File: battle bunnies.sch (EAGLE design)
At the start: 60 parts, among them IC1 CP2104, Q1 mmbt2222, Q2 mmbt2222, SW2 KMR2, U1 PCA9685, U2 SPX3819, U3 MCP73831T-2ACI/OT, X2 ESP-12, X4 20329

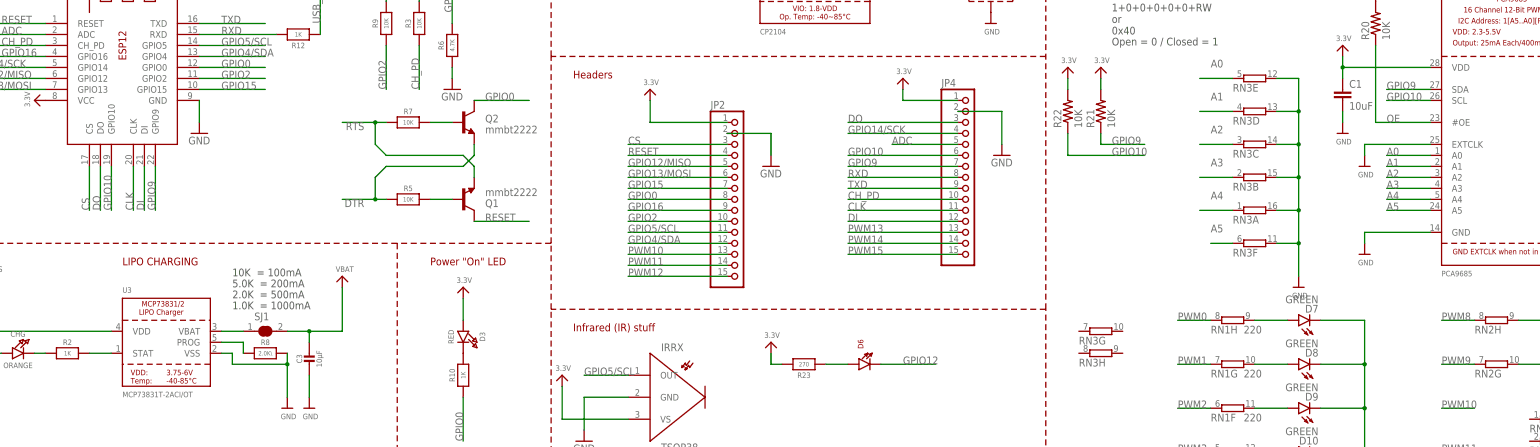
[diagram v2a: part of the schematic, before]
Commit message: Reworking things + the ESP12S is lacking pins present on the schematic (doh)
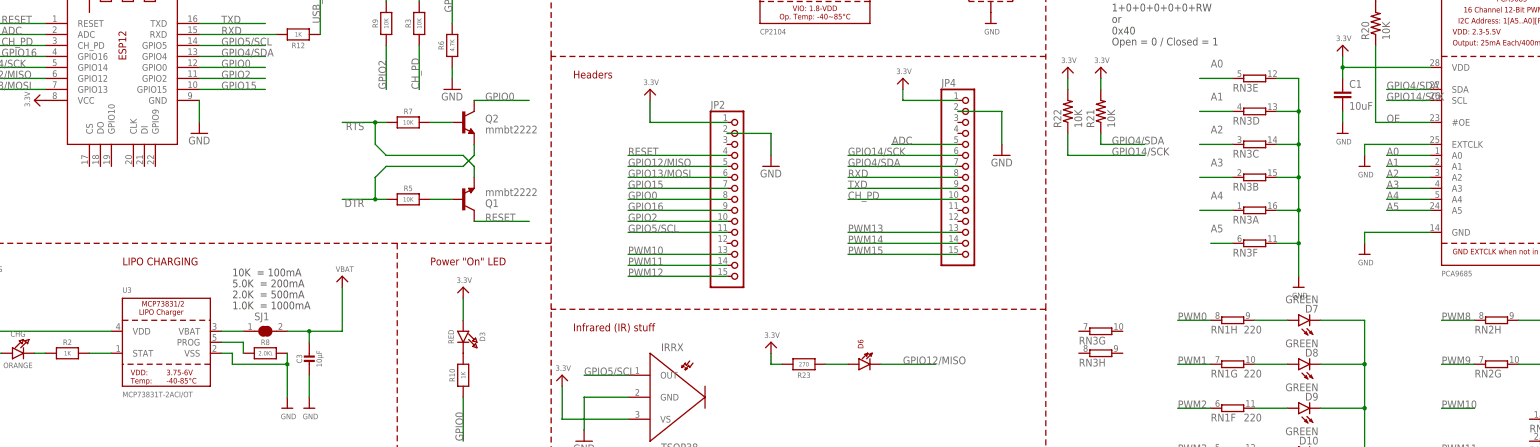
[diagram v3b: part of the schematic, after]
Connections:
- removed net CLK: JP4.11, X2.CLK
- removed net CS: JP2.3, X2.CS
- removed net DI: JP4.12, X2.DI
- removed net DO: JP4.3, X2.DO
- removed net GPIO10: JP4.6, R22.1, U1.SCL, X2.GPIO10
- removed net GPIO12: D6.C
- removed net GPIO9: JP4.7, R21.1, U1.SDA, X2.GPIO9
- net GPIO12/MISO: now also D6.C
- net GPIO14/SCK: now also JP4.6, R22.1, U1.SCL; no longer JP4.4
- net GPIO4/SDA: now also JP4.7, R21.1, U1.SDA; no longer JP2.12
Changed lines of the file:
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@@
 <net name="GPIO4/SDA" class="0">
-<segment>
-<wire x1="154.94" y1="144.78" x2="177.8" y2="144.78" width="0.1524" layer="91"/>
-<label x="154.94" y="144.78" size="1.778" layer="95"/>
-<pinref part="JP2" gate="A" pin="12"/>
-</segment>
 <segment>
 <pinref part="X2" gate="G$1" pin="GPIO4"/>
@@
 <label x="60.96" y="187.96" size="1.778" layer="95"/>
 </segment>
+<segment>
+<wire x1="264.16" y1="167.64" x2="264.16" y2="170.18" width="0.1524" layer="91"/>
+<label x="266.7" y="167.64" size="1.778" layer="95"/>
+<pinref part="R21" gate="G$1" pin="1"/>
+<wire x1="264.16" y1="167.64" x2="274.32" y2="167.64" width="0.1524" layer="91"/>
+</segment>
+<segment>
+<wire x1="340.36" y1="180.34" x2="330.2" y2="180.34" width="0.1524" layer="91"/>
+<label x="330.2" y="180.34" size="1.778" layer="95"/>
+<pinref part="U1" gate="G$1" pin="SDA"/>
+</segment>
+<segment>
+<pinref part="JP4" gate="A" pin="7"/>
+<wire x1="231.14" y1="162.56" x2="205.74" y2="162.56" width="0.1524" layer="91"/>
+<label x="205.74" y="162.56" size="1.778" layer="95"/>
+</segment>
 </net>
 <net name="GPIO2" class="0">
@@
 <wire x1="2.54" y1="185.42" x2="20.32" y2="185.42" width="0.1524" layer="91"/>
 <label x="2.54" y="185.42" size="1.778" layer="95"/>
-</segment>
-<segment>
-<wire x1="231.14" y1="170.18" x2="205.74" y2="170.18" width="0.1524" layer="91"/>
-<label x="205.74" y="170.18" size="1.778" layer="95"/>
-<pinref part="JP4" gate="A" pin="4"/>
-</segment>
-</net>
-<net name="GPIO13/MOSI" class="0">
-<segment>
-<pinref part="X2" gate="G$1" pin="GPIO13"/>
-<wire x1="2.54" y1="180.34" x2="20.32" y2="180.34" width="0.1524" layer="91"/>
-<label x="2.54" y="180.34" size="1.778" layer="95"/>
-</segment>
-<segment>
-<wire x1="177.8" y1="160.02" x2="154.94" y2="160.02" width="0.1524" layer="91"/>
-<label x="154.94" y="160.02" size="1.778" layer="95"/>
-<pinref part="JP2" gate="A" pin="6"/>
-</segment>
-<segment>
-<wire x1="172.72" y1="63.5" x2="190.5" y2="63.5" width="0.1524" layer="91"/>
-<label x="177.8" y="63.5" size="1.778" layer="95"/>
-<pinref part="S2" gate="G$1" pin="2"/>
-</segment>
-</net>
-<net name="GPIO12/MISO" class="0">
-<segment>
-<pinref part="X2" gate="G$1" pin="GPIO12"/>
-<wire x1="20.32" y1="182.88" x2="2.54" y2="182.88" width="0.1524" layer="91"/>
-<label x="2.54" y="182.88" size="1.778" layer="95"/>
-</segment>
-<segment>
-<wire x1="154.94" y1="162.56" x2="177.8" y2="162.56" width="0.1524" layer="91"/>
-<label x="154.94" y="162.56" size="1.778" layer="95"/>
-<pinref part="JP2" gate="A" pin="5"/>
-</segment>
-</net>
-<net name="USB_RX" class="0">
-<segment>
-<pinref part="R12" gate="G$1" pin="1"/>
-<wire x1="83.82" y1="193.04" x2="83.82" y2="205.74" width="0.1524" layer="91"/>
-<label x="83.82" y="195.58" size="1.778" layer="95" rot="R90"/>
-</segment>
-<segment>
-<wire x1="213.36" y1="210.82" x2="226.06" y2="210.82" width="0.1524" layer="91"/>
-<pinref part="IC1" gate="G$1" pin="TXD"/>
-<label x="215.9" y="210.82" size="1.778" layer="95"/>
-</segment>
-</net>
-<net name="N$9" class="0">
-<segment>
-<pinref part="U3" gate="G$1" pin="VBAT"/>
-<pinref part="SJ1" gate="G$1" pin="1"/>
-<wire x1="66.04" y1="124.46" x2="60.96" y2="124.46" width="0.1524" layer="91"/>
-</segment>
-</net>
-<net name="N$11" class="0">
-<segment>
-<wire x1="68.58" y1="241.3" x2="73.66" y2="241.3" width="0.1524" layer="91"/>
-<pinref part="D4" gate="G$1" pin="A"/>
-</segment>
-</net>
-<net name="GPIO10" class="0">
-<segment>
-<pinref part="X2" gate="G$1" pin="GPIO10"/>
-<wire x1="35.56" y1="162.56" x2="35.56" y2="152.4" width="0.1524" layer="91"/>
-<label x="35.56" y="152.4" size="1.778" layer="95" rot="R90"/>
 </segment>
 <segment>
@@
 </segment>
 <segment>
+<pinref part="JP4" gate="A" pin="6"/>
 <wire x1="231.14" y1="165.1" x2="205.74" y2="165.1" width="0.1524" layer="91"/>
 <label x="205.74" y="165.1" size="1.778" layer="95"/>
-<pinref part="JP4" gate="A" pin="6"/>
-</segment>
-</net>
-<net name="GPIO9" class="0">
-<segment>
-<pinref part="X2" gate="G$1" pin="GPIO9"/>
-<wire x1="45.72" y1="162.56" x2="45.72" y2="152.4" width="0.1524" layer="91"/>
-<label x="45.72" y="152.4" size="1.778" layer="95" rot="R90"/>
-</segment>
-<segment>
-<wire x1="264.16" y1="167.64" x2="264.16" y2="170.18" width="0.1524" layer="91"/>
-<label x="266.7" y="167.64" size="1.778" layer="95"/>
-<pinref part="R21" gate="G$1" pin="1"/>
-<wire x1="264.16" y1="167.64" x2="274.32" y2="167.64" width="0.1524" layer="91"/>
-</segment>
-<segment>
-<wire x1="340.36" y1="180.34" x2="330.2" y2="180.34" width="0.1524" layer="91"/>
-<label x="330.2" y="180.34" size="1.778" layer="95"/>
-<pinref part="U1" gate="G$1" pin="SDA"/>
-</segment>
-<segment>
-<wire x1="231.14" y1="162.56" x2="205.74" y2="162.56" width="0.1524" layer="91"/>
-<label x="205.74" y="162.56" size="1.778" layer="95"/>
-<pinref part="JP4" gate="A" pin="7"/>
+</segment>
+</net>
+<net name="GPIO13/MOSI" class="0">
+<segment>
+<pinref part="X2" gate="G$1" pin="GPIO13"/>
+<wire x1="2.54" y1="180.34" x2="20.32" y2="180.34" width="0.1524" layer="91"/>
+<label x="2.54" y="180.34" size="1.778" layer="95"/>
+</segment>
+<segment>
+<wire x1="177.8" y1="160.02" x2="154.94" y2="160.02" width="0.1524" layer="91"/>
+<label x="154.94" y="160.02" size="1.778" layer="95"/>
+<pinref part="JP2" gate="A" pin="6"/>
+</segment>
+<segment>
+<wire x1="172.72" y1="63.5" x2="190.5" y2="63.5" width="0.1524" layer="91"/>
+<label x="177.8" y="63.5" size="1.778" layer="95"/>
+<pinref part="S2" gate="G$1" pin="2"/>
+</segment>
+</net>
+<net name="GPIO12/MISO" class="0">
+<segment>
+<pinref part="X2" gate="G$1" pin="GPIO12"/>
+<wire x1="20.32" y1="182.88" x2="2.54" y2="182.88" width="0.1524" layer="91"/>
+<label x="2.54" y="182.88" size="1.778" layer="95"/>
+</segment>
+<segment>
+<wire x1="154.94" y1="162.56" x2="177.8" y2="162.56" width="0.1524" layer="91"/>
+<label x="154.94" y="162.56" size="1.778" layer="95"/>
+<pinref part="JP2" gate="A" pin="5"/>
+</segment>
+<segment>
+<pinref part="D6" gate="G$1" pin="C"/>
+<wire x1="213.36" y1="116.84" x2="226.06" y2="116.84" width="0.1524" layer="91"/>
+<label x="218.44" y="116.84" size="1.778" layer="95"/>
+</segment>
+</net>
+<net name="USB_RX" class="0">
+<segment>
+<pinref part="R12" gate="G$1" pin="1"/>
+<wire x1="83.82" y1="193.04" x2="83.82" y2="205.74" width="0.1524" layer="91"/>
+<label x="83.82" y="195.58" size="1.778" layer="95" rot="R90"/>
+</segment>
+<segment>
+<wire x1="213.36" y1="210.82" x2="226.06" y2="210.82" width="0.1524" layer="91"/>
+<pinref part="IC1" gate="G$1" pin="TXD"/>
+<label x="215.9" y="210.82" size="1.778" layer="95"/>
+</segment>
+</net>
+<net name="N$9" class="0">
+<segment>
+<pinref part="U3" gate="G$1" pin="VBAT"/>
+<pinref part="SJ1" gate="G$1" pin="1"/>
+<wire x1="66.04" y1="124.46" x2="60.96" y2="124.46" width="0.1524" layer="91"/>
+</segment>
+</net>
+<net name="N$11" class="0">
+<segment>
+<wire x1="68.58" y1="241.3" x2="73.66" y2="241.3" width="0.1524" layer="91"/>
+<pinref part="D4" gate="G$1" pin="A"/>
 </segment>
 </net>
@@
 </segment>
 </net>
-<net name="GPIO12" class="0">
-<segment>
-<pinref part="D6" gate="G$1" pin="C"/>
-<wire x1="213.36" y1="116.84" x2="226.06" y2="116.84" width="0.1524" layer="91"/>
-<label x="218.44" y="116.84" size="1.778" layer="95"/>
-</segment>
-</net>
-<net name="CS" class="0">
-<segment>
-<pinref part="X2" gate="G$1" pin="CS"/>
-<wire x1="30.48" y1="162.56" x2="30.48" y2="152.4" width="0.1524" layer="91"/>
-<label x="30.48" y="152.4" size="1.778" layer="95" rot="R90"/>
-</segment>
-<segment>
-<pinref part="JP2" gate="A" pin="3"/>
-<wire x1="177.8" y1="167.64" x2="154.94" y2="167.64" width="0.1524" layer="91"/>
-<label x="154.94" y="167.64" size="1.778" layer="95"/>
-</segment>
-</net>
-<net name="DO" class="0">
-<segment>
-<pinref part="X2" gate="G$1" pin="DO"/>
-<wire x1="33.02" y1="162.56" x2="33.02" y2="152.4" width="0.1524" layer="91"/>
-<label x="33.02" y="152.4" size="1.778" layer="95" rot="R90"/>
-</segment>
-<segment>
-<pinref part="JP4" gate="A" pin="3"/>
-<wire x1="231.14" y1="172.72" x2="205.74" y2="172.72" width="0.1524" layer="91"/>
-<label x="205.74" y="172.72" size="1.778" layer="95"/>
-</segment>
-</net>
-<net name="CLK" class="0">
-<segment>
-<pinref part="X2" gate="G$1" pin="CLK"/>
-<wire x1="40.64" y1="162.56" x2="40.64" y2="152.4" width="0.1524" layer="91"/>
-<label x="40.64" y="152.4" size="1.778" layer="95" rot="R90"/>
-</segment>
-<segment>
-<wire x1="231.14" y1="152.4" x2="205.74" y2="152.4" width="0.1524" layer="91"/>
-<label x="205.74" y="152.4" size="1.778" layer="95"/>
-<pinref part="JP4" gate="A" pin="11"/>
-</segment>
-</net>
-<net name="DI" class="0">
-<segment>
-<pinref part="X2" gate="G$1" pin="DI"/>
-<wire x1="43.18" y1="162.56" x2="43.18" y2="152.4" width="0.1524" layer="91"/>
-<label x="43.18" y="152.4" size="1.778" layer="95" rot="R90"/>
-</segment>
-<segment>
-<wire x1="231.14" y1="149.86" x2="205.74" y2="149.86" width="0.1524" layer="91"/>
-<label x="205.74" y="149.86" size="1.778" layer="95"/>
-<pinref part="JP4" gate="A" pin="12"/>
-</segment>
-</net>

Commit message: more cleanups
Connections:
- net GPIO0: now also JP2.3; no longer JP2.8
- net GPIO12/MISO: now also JP2.12; no longer JP2.5
- net GPIO2: now also JP2.4; no longer JP2.10
- net RESET: now also JP2.5; no longer JP2.4
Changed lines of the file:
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@@
 <?xml version="1.0" encoding="utf-8"?>
 <!DOCTYPE eagle SYSTEM "eagle.dtd">
-<eagle version="7.6.0">
+<eagle version="7.7.0">
 <drawing>
 <settings>
@@
 </segment>
 <segment>
-<pinref part="JP2" gate="A" pin="4"/>
-<wire x1="177.8" y1="165.1" x2="154.94" y2="165.1" width="0.1524" layer="91"/>
-<label x="154.94" y="165.1" size="1.778" layer="95"/>
+<wire x1="177.8" y1="162.56" x2="154.94" y2="162.56" width="0.1524" layer="91"/>
+<label x="154.94" y="162.56" size="1.778" layer="95"/>
+<pinref part="JP2" gate="A" pin="5"/>
 </segment>
 </net>
@@
 </segment>
 <segment>
-<wire x1="177.8" y1="154.94" x2="154.94" y2="154.94" width="0.1524" layer="91"/>
-<label x="154.94" y="154.94" size="1.778" layer="95"/>
-<pinref part="JP2" gate="A" pin="8"/>
+<pinref part="JP2" gate="A" pin="3"/>
+<wire x1="177.8" y1="167.64" x2="154.94" y2="167.64" width="0.1524" layer="91"/>
+<label x="154.94" y="167.64" size="1.778" layer="95"/>
 </segment>
 </net>
@@
 </segment>
 <segment>
-<wire x1="154.94" y1="149.86" x2="177.8" y2="149.86" width="0.1524" layer="91"/>
-<label x="154.94" y="149.86" size="1.778" layer="95"/>
-<pinref part="JP2" gate="A" pin="10"/>
+<wire x1="177.8" y1="165.1" x2="154.94" y2="165.1" width="0.1524" layer="91"/>
+<label x="154.94" y="165.1" size="1.778" layer="95"/>
+<pinref part="JP2" gate="A" pin="4"/>
 </segment>
 </net>
@@
 </segment>
 <segment>
-<wire x1="154.94" y1="162.56" x2="177.8" y2="162.56" width="0.1524" layer="91"/>
-<label x="154.94" y="162.56" size="1.778" layer="95"/>
-<pinref part="JP2" gate="A" pin="5"/>
-</segment>
-<segment>
 <pinref part="D6" gate="G$1" pin="C"/>
 <wire x1="213.36" y1="116.84" x2="226.06" y2="116.84" width="0.1524" layer="91"/>
 <label x="218.44" y="116.84" size="1.778" layer="95"/>
 </segment>
-</net>
+<segment>
+<pinref part="JP2" gate="A" pin="12"/>
+<wire x1="177.8" y1="144.78" x2="154.94" y2="144.78" width="0.1524" layer="91"/>
+<label x="154.94" y="144.78" size="1.778" layer="95"/>
+</segment>
+</net>

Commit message: Finally moved things around enough to make it all work
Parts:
- removed C2: 10uF, microbuilder:CAP_CERAMIC0805-NOOUTLINE
- added U$17: AAA3, Warthog9-Batteries:AAA3
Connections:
- net N$6 renamed USBD_P
- net N$7 renamed USBD_N
- net 3.3V: no longer C2.1
- net GND: no longer C2.2
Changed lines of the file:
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@@
 <class number="0" name="default" width="0" drill="0">
+</class>
+<class number="1" name="USB1" width="0" drill="0">
 </class>
 </classes>
@@
 <part name="U$11" library="microbuilder" deviceset="GND" device=""/>
 <part name="U$12" library="microbuilder" deviceset="GND" device=""/>
-<part name="C2" library="microbuilder" deviceset="CAP_CERAMIC" device="0805-NOOUTLINE" value="10uF"/>
-<part name="U$17" library="microbuilder" deviceset="GND" device=""/>
 <part name="U$18" library="microbuilder" deviceset="VBUS" device=""/>
 <part name="R5" library="microbuilder" deviceset="RESISTOR" device="_0603_NOOUT" value="10K"/>
@@
 <part name="RN2" library="resistor-dil" deviceset="8R-N" device="EXB2HV"/>
 <part name="RN3" library="resistor-dil" deviceset="8R-N" device="EXB2HV"/>
+<part name="U$17" library="Warthog9-Batteries" deviceset="AAA3" device=""/>
 </parts>
 <sheets>
@@
 <instance part="U$11" gate="G$1" x="165.1" y="205.74"/>
 <instance part="U$12" gate="G$1" x="180.34" y="226.06"/>
-<instance part="C2" gate="G$1" x="175.26" y="233.68"/>
-<instance part="U$17" gate="G$1" x="175.26" y="226.06"/>
 <instance part="U$18" gate="G$1" x="167.64" y="226.06"/>
 <instance part="R5" gate="G$1" x="104.14" y="154.94"/>
@@
 <instance part="RN3" gate="G" x="264.16" y="124.46"/>
 <instance part="RN3" gate="H" x="264.16" y="119.38"/>
+<instance part="U$17" gate="G$1" x="93.98" y="254" rot="R90"/>
 </instances>
 <busses>
@@
 <wire x1="182.88" y1="231.14" x2="180.34" y2="231.14" width="0.1524" layer="91"/>
 <wire x1="180.34" y1="231.14" x2="180.34" y2="228.6" width="0.1524" layer="91"/>
-</segment>
-<segment>
-<pinref part="C2" gate="G$1" pin="2"/>
-<pinref part="U$17" gate="G$1" pin="GND"/>
-<wire x1="175.26" y1="231.14" x2="175.26" y2="228.6" width="0.1524" layer="91"/>
 </segment>
 <segment>
@@
 </segment>
 <segment>
-<pinref part="C2" gate="G$1" pin="1"/>
-<wire x1="175.26" y1="241.3" x2="175.26" y2="238.76" width="0.1524" layer="91"/>
 <pinref part="IC1" gate="G$1" pin="REGIN"/>
 <wire x1="182.88" y1="241.3" x2="175.26" y2="241.3" width="0.1524" layer="91"/>
@@
 </segment>
 </net>
-<net name="N$6" class="0">
+<net name="USBD_P" class="1">
 <segment>
 <pinref part="X4" gate="G$1" pin="D+"/>
@@
 </segment>
 </net>
-<net name="N$7" class="0">
+<net name="USBD_N" class="1">
 <segment>
 <pinref part="X4" gate="G$1" pin="D-"/>

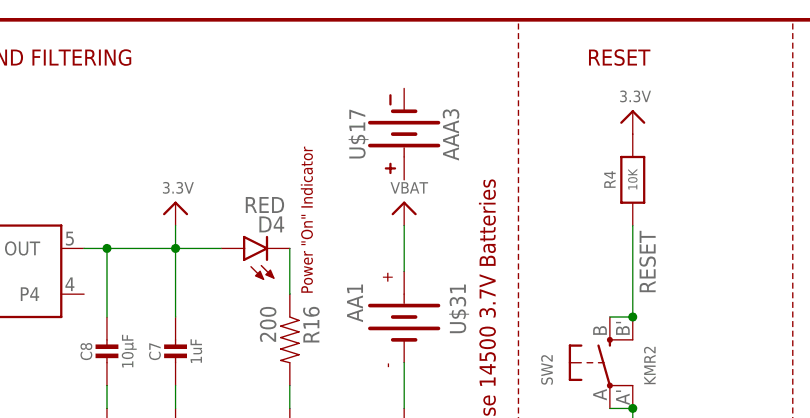
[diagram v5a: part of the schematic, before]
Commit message: Just adding some silk
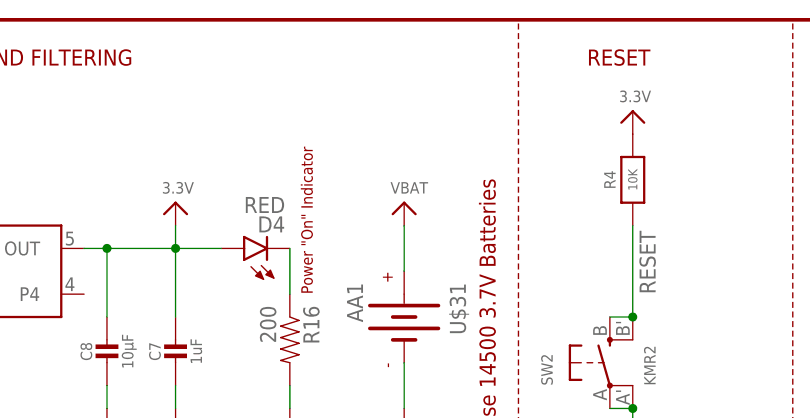
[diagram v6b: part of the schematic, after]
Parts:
- removed U$17: AAA3, Warthog9-Batteries:AAA3
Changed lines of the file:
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@@
 <part name="RN2" library="resistor-dil" deviceset="8R-N" device="EXB2HV"/>
 <part name="RN3" library="resistor-dil" deviceset="8R-N" device="EXB2HV"/>
-<part name="U$17" library="Warthog9-Batteries" deviceset="AAA3" device=""/>
 </parts>
 <sheets>
@@
 <instance part="RN3" gate="G" x="264.16" y="124.46"/>
 <instance part="RN3" gate="H" x="264.16" y="119.38"/>
-<instance part="U$17" gate="G$1" x="93.98" y="254" rot="R90"/>
 </instances>
 <busses>
